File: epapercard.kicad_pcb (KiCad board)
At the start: 2 copper layers, 88.9 x 49.5 mm, 47 parts, among them P1 PROG, P2 A120699CT, Q1 2N7002KW, Q2 BSS84W, Q3 BSS84W, Q4 BSS84W, Q5 2N7002KW, Q6 2N7002KW, Q7 2N7002KW, SW1 SW_PUSH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

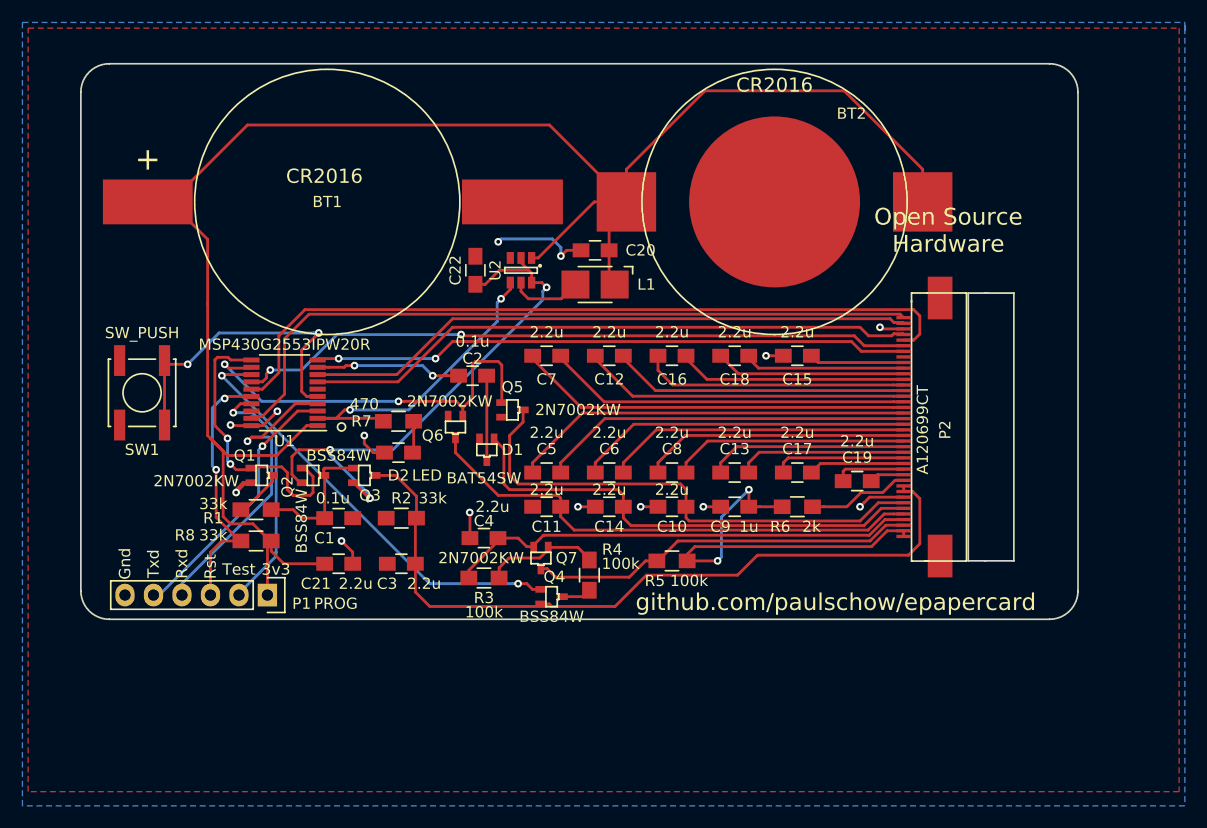
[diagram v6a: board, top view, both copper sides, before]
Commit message: Silk cleanup
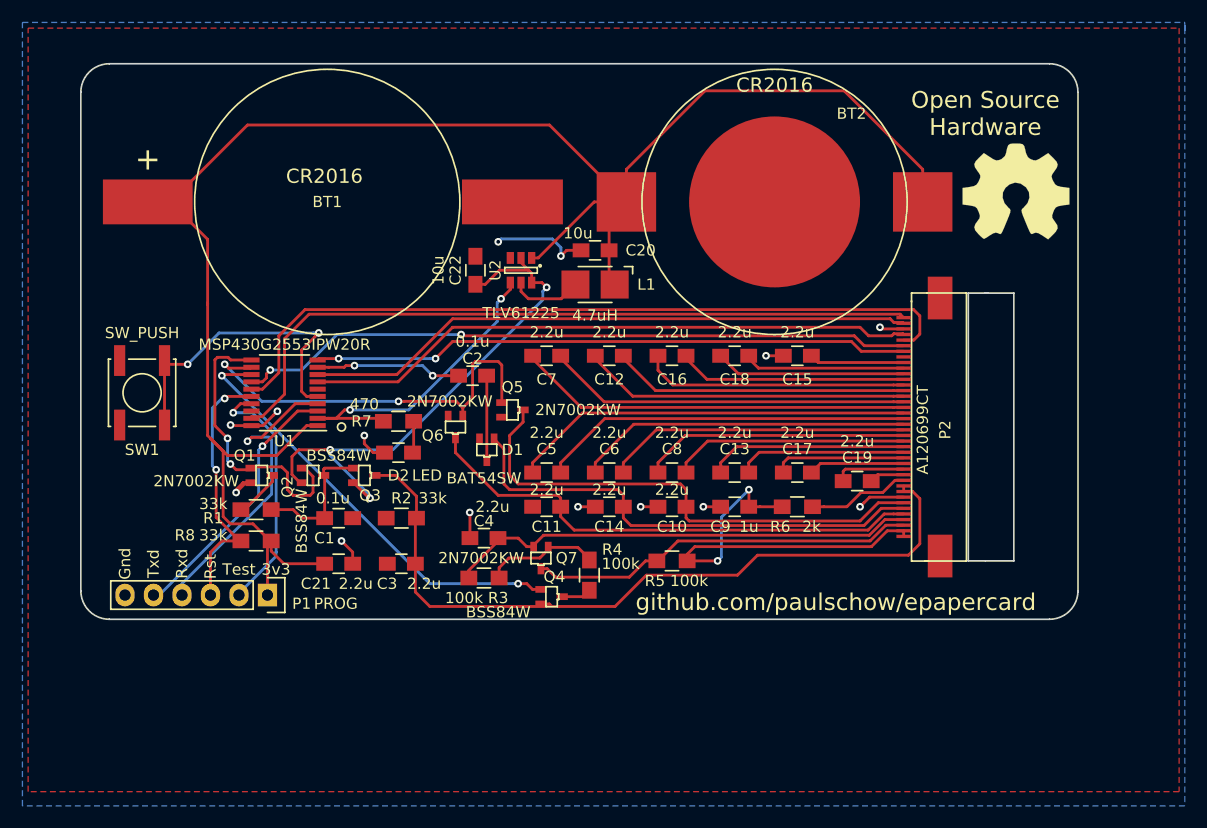
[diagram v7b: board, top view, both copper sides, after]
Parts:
- added G***: LOGO, footprint:oshlogo, F.Cu at (106.9, 41.1)
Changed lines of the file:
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@@
     (tracks 501)
     (zones 0)
-    (modules 47)
+    (modules 48)
     (nets 56)
   )
@@
       (effects (font (size 1 1) (thickness 0.15)))
     )
-    (fp_text value BSS84W (at -1.778 0 180) (layer F.SilkS)
+    (fp_text value BSS84W (at -1.38176 -4.75996 180) (layer F.SilkS)
       (effects (font (size 1 1) (thickness 0.15)))
     )
@@
     (tags "resistor 0805")
     (attr smd)
-    (fp_text reference R3 (at 0 -1.778 180) (layer F.SilkS)
-      (effects (font (size 1 1) (thickness 0.15)))
-    )
-    (fp_text value 100k (at 0 -3.048 180) (layer F.SilkS)
+    (fp_text reference R3 (at -1.27 -1.778 180) (layer F.SilkS)
+      (effects (font (size 1 1) (thickness 0.15)))
+    )
+    (fp_text value 100k (at 1.778 -1.778 180) (layer F.SilkS)
       (effects (font (size 1 1) (thickness 0.15)))
     )
@@
       (effects (font (size 1 1) (thickness 0.15)))
     )
-    (fp_text value 10u (at 0 2.1) (layer F.Fab)
+    (fp_text value 10u (at -1.524 -1.524) (layer F.SilkS)
       (effects (font (size 1 1) (thickness 0.15)))
     )
@@
       (effects (font (size 1 1) (thickness 0.15)))
     )
-    (fp_text value 10u (at 0 2.1 270) (layer F.Fab)
+    (fp_text value 10u (at 0 3.302 270) (layer F.SilkS)
       (effects (font (size 1 1) (thickness 0.15)))
     )
@@
       (effects (font (size 1 1) (thickness 0.15)))
     )
-    (fp_text value 4.7uH (at 0 -2.75 180) (layer F.Fab)
+    (fp_text value 4.7uH (at 0 -2.75 180) (layer F.SilkS)
       (effects (font (size 1 1) (thickness 0.15)))
     )
@@
       (effects (font (size 1 1) (thickness 0.15)))
     )
-    (fp_text value TLV61225 (at 0 2.9 270) (layer F.Fab)
+    (fp_text value TLV61225 (at 3.81 0 360) (layer F.SilkS)
       (effects (font (size 1 1) (thickness 0.15)))
     )
@@
     )
   )
+  (module footprint:oshlogo (layer F.Cu)
+    (at 106.934 41.148)
+    (fp_text reference G*** (at 0 0) (layer F.SilkS) hide
+      (effects (font (thickness 0.3)))
+    )
+    (fp_text value LOGO (at 0.75 0) (layer F.SilkS) hide
+      (effects (font (thickness 0.3)))
+    )
+    (fp_poly (pts (xy 0.317705 -4.183579) (xy 0.544109 -4.124546) (xy 0.673891 -3.958747) (xy 0.765227 -3.631029)
+      (xy 0.822256 -3.351294) (xy 1.004849 -2.970441) (xy 1.218713 -2.811544) (xy 1.497135 -2.701771)
+      (xy 1.716418 -2.692099) (xy 1.968617 -2.799064) (xy 2.29365 -3.004638) (xy 2.803854 -3.342275)
+      (xy 3.243427 -2.916225) (xy 3.549387 -2.582693) (xy 3.658144 -2.316975) (xy 3.577739 -2.037242)
+      (xy 3.360965 -1.719844) (xy 3.163229 -1.440412) (xy 3.108189 -1.241179) (xy 3.181093 -1.00303)
+      (xy 3.253056 -0.84861) (xy 3.416148 -0.567891) (xy 3.619636 -0.416277) (xy 3.957654 -0.333238)
+      (xy 4.083091 -0.314875) (xy 4.699 -0.230166) (xy 4.699 1.246165) (xy 4.079416 1.331379)
+      (xy 3.69666 1.401585) (xy 3.478501 1.517329) (xy 3.336057 1.740407) (xy 3.273089 1.891995)
+      (xy 3.164193 2.213567) (xy 3.175692 2.428905) (xy 3.32402 2.663527) (xy 3.384042 2.739448)
+      (xy 3.613613 3.08782) (xy 3.651214 3.374559) (xy 3.488315 3.672045) (xy 3.243427 3.932224)
+      (xy 2.803854 4.358274) (xy 2.288699 4.017361) (xy 1.934919 3.811794) (xy 1.693066 3.756767)
+      (xy 1.529479 3.807067) (xy 1.406775 3.871121) (xy 1.314733 3.881204) (xy 1.226409 3.80024)
+      (xy 1.114855 3.591156) (xy 0.953127 3.216876) (xy 0.757799 2.745306) (xy 0.559401 2.259558)
+      (xy 0.451113 1.952495) (xy 0.42568 1.768203) (xy 0.475845 1.650769) (xy 0.594352 1.544281)
+      (xy 0.60123 1.538806) (xy 0.965551 1.118879) (xy 1.130188 0.634971) (xy 1.087711 0.148892)
+      (xy 0.830692 -0.277548) (xy 0.820759 -0.287604) (xy 0.345041 -0.620084) (xy -0.150735 -0.703278)
+      (xy -0.641552 -0.537868) (xy -1.003805 -0.237833) (xy -1.228768 0.173503) (xy -1.250693 0.652831)
+      (xy -1.08031 1.130963) (xy -0.728351 1.538711) (xy -0.728231 1.538806) (xy -0.606796 1.646123)
+      (xy -0.553374 1.76185) (xy -0.575222 1.941899) (xy -0.679594 2.242183) (xy -0.873747 2.718614)
+      (xy -0.8848 2.745306) (xy -1.109814 3.28781) (xy -1.261956 3.633815) (xy -1.368251 3.820349)
+      (xy -1.455727 3.884444) (xy -1.551408 3.863129) (xy -1.658799 3.805826) (xy -1.87052 3.752967)
+      (xy -2.127611 3.839816) (xy -2.379072 3.995983) (xy -2.679045 4.189814) (xy -2.885088 4.304567)
+      (xy -2.925568 4.318) (xy -3.049504 4.234807) (xy -3.279485 4.024325) (xy -3.404087 3.899203)
+      (xy -3.696188 3.551965) (xy -3.787831 3.272477) (xy -3.686254 2.982275) (xy -3.511043 2.739448)
+      (xy -3.326149 2.480552) (xy -3.282169 2.272143) (xy -3.362669 1.988704) (xy -3.40009 1.891995)
+      (xy -3.537453 1.600577) (xy -3.7106 1.444258) (xy -4.008413 1.361238) (xy -4.206417 1.331379)
+      (xy -4.826 1.246165) (xy -4.826 -0.230166) (xy -4.210092 -0.314875) (xy -3.820068 -0.389824)
+      (xy -3.589782 -0.517139) (xy -3.425101 -0.75735) (xy -3.380057 -0.84861) (xy -3.253549 -1.144259)
+      (xy -3.248236 -1.346512) (xy -3.378873 -1.57448) (xy -3.487966 -1.719844) (xy -3.725969 -2.078023)
+      (xy -3.781783 -2.351198) (xy -3.647369 -2.621197) (xy -3.370428 -2.916225) (xy -2.930855 -3.342275)
+      (xy -2.420651 -3.004638) (xy -2.062343 -2.780487) (xy -1.818531 -2.687628) (xy -1.59716 -2.709524)
+      (xy -1.345714 -2.811544) (xy -1.053565 -3.077021) (xy -0.949257 -3.351294) (xy -0.85383 -3.795725)
+      (xy -0.753051 -4.046865) (xy -0.588744 -4.159866) (xy -0.302728 -4.189882) (xy -0.063501 -4.191)
+      (xy 0.317705 -4.183579)) (layer F.SilkS) (width 0.01))
+  )
   (gr_line (start 23.495 76.835) (end 23.495 32.3596) (angle 90) (layer Edge.Cuts) (width 0.15))
   (gr_line (start 112.395 32.4104) (end 112.395 76.9112) (angle 90) (layer Edge.Cuts) (width 0.15))
@@
   (gr_line (start 102.616 74.168) (end 104.14 74.168) (angle 90) (layer Edge.Cuts) (width 0.15))
   (gr_line (start 102.616 50.292) (end 104.394 50.292) (angle 90) (layer Edge.Cuts) (width 0.15))
-  (gr_text "Open Source\nHardware" (at 100.838 44.704) (layer F.SilkS)
+  (gr_text "Open Source\nHardware" (at 104.14 34.29) (layer F.SilkS)
     (effects (font (size 1.5 1.5) (thickness 0.3)))
   )
-  (gr_text 3v3 (at 40.894 74.93 360) (layer F.SilkS)
+  (gr_text 3v3 (at 40.894 74.93) (layer F.SilkS)
     (effects (font (size 1.016 1.016) (thickness 0.1524)))
   )
-  (gr_text Test (at 37.592 74.93 360) (layer F.SilkS)
+  (gr_text Test (at 37.592 74.93) (layer F.SilkS)
     (effects (font (size 1.016 1.016) (thickness 0.1524)))
   )

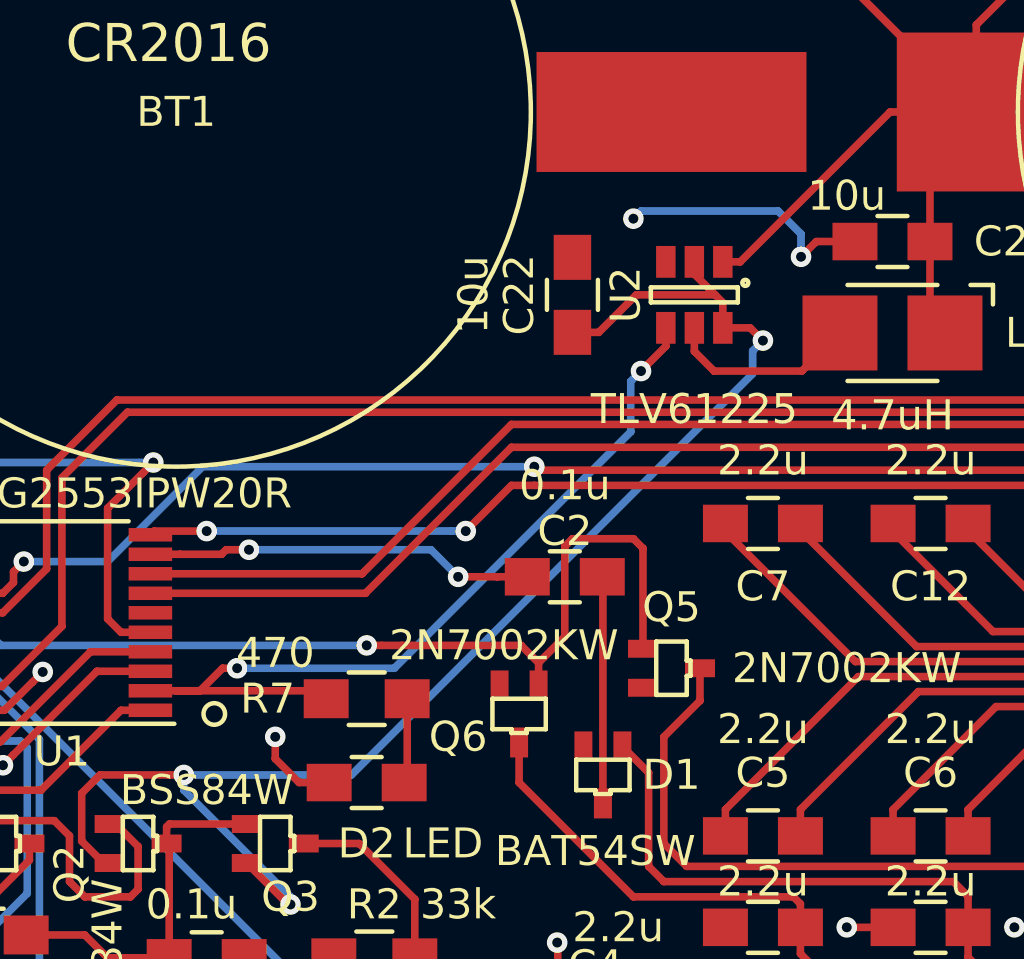
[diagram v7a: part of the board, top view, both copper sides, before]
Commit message: Fixed TLV61225 footprint
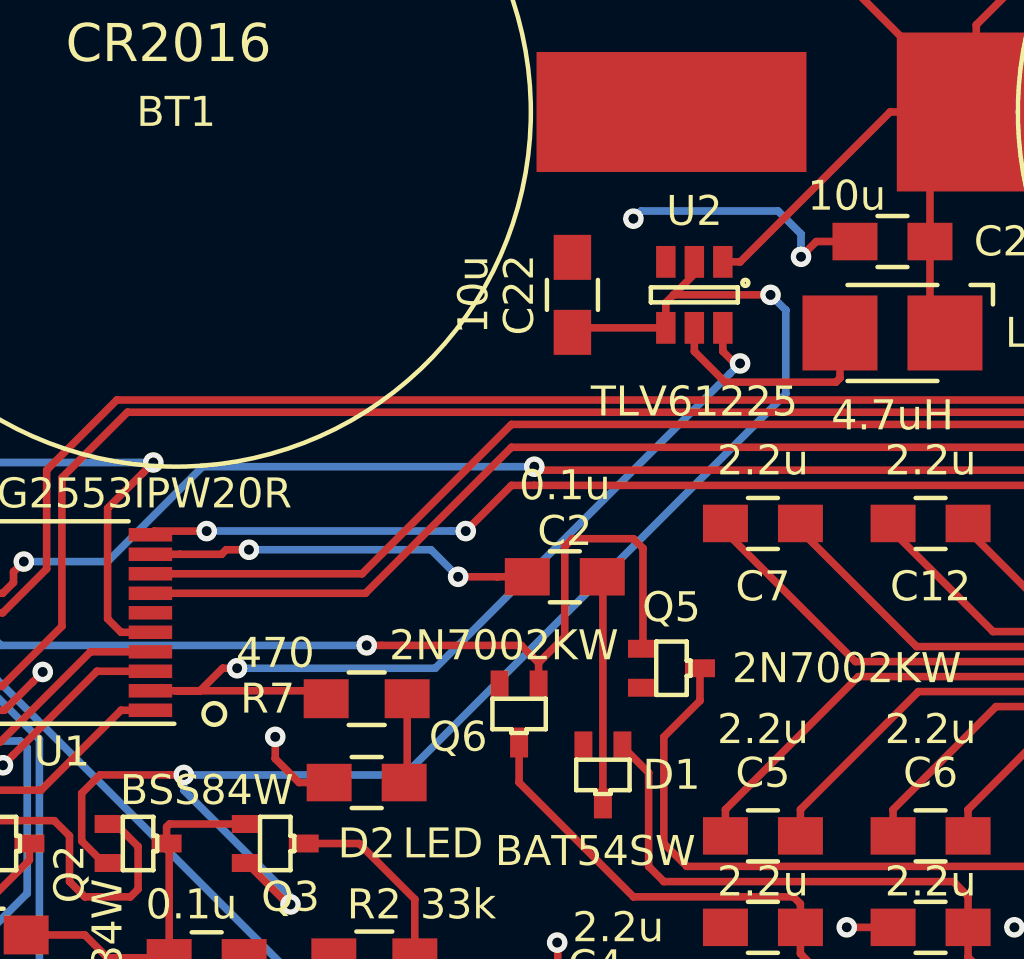
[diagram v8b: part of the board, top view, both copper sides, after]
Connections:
- U2 pad 4: /led -> /Vboost
- U2 pad 6: /Vboost -> /led
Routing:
- net /Vboost: track 50.1 -> 52.8 mm
- net /led: track 28.7 -> 30.8 mm
- net Net-(L1-Pad2): track 6.44 -> 7.62 mm
